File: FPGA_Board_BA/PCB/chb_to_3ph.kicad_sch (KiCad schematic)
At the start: 1 part, among them J103 Plug_Termincal_8pin

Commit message: lots of work
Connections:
- net Ph_A1_out renamed M_PHA
- net Ph_B1_out renamed M_PHB
- net Ph_C1_out renamed M_PHC
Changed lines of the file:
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@@
 		)
 	)
-	(wire
-		(pts
-			(xy 134.62 92.71) (xy 138.43 92.71)
-		)
-		(stroke
-			(width 0)
-			(type default)
-		)
-	)
-	(wire
-		(pts
-			(xy 118.11 92.71) (xy 121.92 92.71)
-		)
-		(stroke
-			(width 0)
-			(type default)
-		)
-	)
-	(wire
-		(pts
-			(xy 134.62 87.63) (xy 138.43 87.63)
-		)
-		(stroke
-			(width 0)
-			(type default)
-		)
-	)
-	(wire
-		(pts
-			(xy 134.62 85.09) (xy 138.43 85.09)
-		)
-		(stroke
-			(width 0)
-			(type default)
-		)
-	)
-	(wire
-		(pts
-			(xy 118.11 87.63) (xy 121.92 87.63)
-		)
-		(stroke
-			(width 0)
-			(type default)
-		)
-	)
-	(wire
-		(pts
-			(xy 134.62 90.17) (xy 138.43 90.17)
-		)
-		(stroke
-			(width 0)
-			(type default)
-		)
-	)
-	(wire
-		(pts
-			(xy 118.11 90.17) (xy 121.92 90.17)
-		)
-		(stroke
-			(width 0)
-			(type default)
-		)
-	)
-	(wire
-		(pts
-			(xy 118.11 85.09) (xy 121.92 85.09)
-		)
-		(stroke
-			(width 0)
-			(type default)
+	(junction
+		(at 139.7 87.63)
+		(diameter 0)
+		(color 0 0 0 0)
+	)
+	(junction
+		(at 137.16 90.17)
+		(diameter 0)
+		(color 0 0 0 0)
+	)
+	(junction
+		(at 142.24 85.09)
+		(diameter 0)
+		(color 0 0 0 0)
+	)
+	(wire
+		(pts
+			(xy 144.78 113.03) (xy 139.7 113.03)
+		)
+		(stroke
+			(width 0)
+			(type default)
+		)
+	)
+	(wire
+		(pts
+			(xy 134.62 92.71) (xy 146.05 92.71)
+		)
+		(stroke
+			(width 0)
+			(type default)
+		)
+	)
+	(wire
+		(pts
+			(xy 144.78 118.11) (xy 137.16 118.11)
+		)
+		(stroke
+			(width 0)
+			(type default)
+		)
+	)
+	(wire
+		(pts
+			(xy 110.49 92.71) (xy 121.92 92.71)
+		)
+		(stroke
+			(width 0)
+			(type default)
+		)
+	)
+	(wire
+		(pts
+			(xy 134.62 87.63) (xy 139.7 87.63)
+		)
+		(stroke
+			(width 0)
+			(type default)
+		)
+	)
+	(wire
+		(pts
+			(xy 139.7 87.63) (xy 146.05 87.63)
+		)
+		(stroke
+			(width 0)
+			(type default)
+		)
+	)
+	(wire
+		(pts
+			(xy 137.16 118.11) (xy 137.16 90.17)
+		)
+		(stroke
+			(width 0)
+			(type default)
+		)
+	)
+	(wire
+		(pts
+			(xy 134.62 85.09) (xy 142.24 85.09)
+		)
+		(stroke
+			(width 0)
+			(type default)
+		)
+	)
+	(wire
+		(pts
+			(xy 142.24 85.09) (xy 146.05 85.09)
+		)
+		(stroke
+			(width 0)
+			(type default)
+		)
+	)
+	(wire
+		(pts
+			(xy 110.49 87.63) (xy 121.92 87.63)
+		)
+		(stroke
+			(width 0)
+			(type default)
+		)
+	)
+	(wire
+		(pts
+			(xy 134.62 90.17) (xy 137.16 90.17)
+		)
+		(stroke
+			(width 0)
+			(type default)
+		)
+	)
+	(wire
+		(pts
+			(xy 144.78 107.95) (xy 142.24 107.95)
+		)
+		(stroke
+			(width 0)
+			(type default)
+		)
+	)
+	(wire
+		(pts
+			(xy 110.49 90.17) (xy 121.92 90.17)
+		)
+		(stroke
+			(width 0)
+			(type default)
+		)
+	)
+	(wire
+		(pts
+			(xy 142.24 107.95) (xy 142.24 85.09)
+		)
+		(stroke
+			(width 0)
+			(type default)
+		)
+	)
+	(wire
+		(pts
+			(xy 110.49 85.09) (xy 121.92 85.09)
+		)
+		(stroke
+			(width 0)
+			(type default)
+		)
+	)
+	(wire
+		(pts
+			(xy 137.16 90.17) (xy 146.05 90.17)
+		)
+		(stroke
+			(width 0)
+			(type default)
+		)
+	)
+	(wire
+		(pts
+			(xy 139.7 113.03) (xy 139.7 87.63)
+		)
+		(stroke
+			(width 0)
+			(type default)
+		)
+	)
+	(global_label "M_PHB"
+		(shape bidirectional)
+		(at 144.78 113.03 0)
+		(fields_autoplaced yes)
+		(effects
+			(font
+				(size 1.27 1.27)
+			)
+			(justify left)
+		)
+		(property "Intersheetrefs" "${INTERSHEET_REFS}"
+			(at 155.166 113.03 0)
+			(effects
+				(font
+					(size 1.27 1.27)
+				)
+				(justify left)
+				(hide yes)
+			)
+		)
+	)
+	(global_label "M_PHA"
+		(shape bidirectional)
+		(at 144.78 107.95 0)
+		(fields_autoplaced yes)
+		(effects
+			(font
+				(size 1.27 1.27)
+			)
+			(justify left)
+		)
+		(property "Intersheetrefs" "${INTERSHEET_REFS}"
+			(at 154.9846 107.95 0)
+			(effects
+				(font
+					(size 1.27 1.27)
+				)
+				(justify left)
+				(hide yes)
+			)
+		)
+	)
+	(global_label "M_PHC"
+		(shape bidirectional)
+		(at 144.78 118.11 0)
+		(fields_autoplaced yes)
+		(effects
+			(font
+				(size 1.27 1.27)
+			)
+			(justify left)
+		)
+		(property "Intersheetrefs" "${INTERSHEET_REFS}"
+			(at 155.166 118.11 0)
+			(effects
+				(font
+					(size 1.27 1.27)
+				)
+				(justify left)
+				(hide yes)
+			)
 		)
 	)
 	(hierarchical_label "Ph_A1_out"
 		(shape input)
-		(at 138.43 85.09 0)
+		(at 146.05 85.09 0)
 		(effects
 			(font
@@
 	(hierarchical_label "Ph_C1_out"
 		(shape input)
-		(at 138.43 90.17 0)
+		(at 146.05 90.17 0)
 		(effects
 			(font
@@
 	(hierarchical_label "Ph_D1_out"
 		(shape input)
-		(at 138.43 92.71 0)
+		(at 146.05 92.71 0)
 		(effects
 			(font
@@
 	(hierarchical_label "Ph_A2_out"
 		(shape input)
-		(at 118.11 85.09 180)
+		(at 110.49 85.09 180)
 		(effects
 			(font
@@
 	(hierarchical_label "Ph_D2_out"
 		(shape input)
-		(at 118.11 92.71 180)
+		(at 110.49 92.71 180)
 		(effects
 			(font
@@
 	(hierarchical_label "Ph_B2_out"
 		(shape input)
-		(at 118.11 87.63 180)
+		(at 110.49 87.63 180)
 		(effects
 			(font
@@
 	(hierarchical_label "Ph_C2_out"
 		(shape input)
-		(at 118.11 90.17 180)
+		(at 110.49 90.17 180)
 		(effects
 			(font
@@
 	(hierarchical_label "Ph_B1_out"
 		(shape input)
-		(at 138.43 87.63 0)
-		(effects
-			(font
+		(at 146.05 87.63 0)
+		(effects
+			(font

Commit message: work
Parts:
- renumbered J103 to J9
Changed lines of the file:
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@@
 		(dnp no)
 		(fields_autoplaced yes)
-		(property "Reference" "J103"
+		(property "Reference" "J9"
 			(at 128.27 78.74 0)
 			(effects
@@
 			(project "FPGA_Board_BA"
 				(path "/fd7503bc-e7fc-4766-b224-3d1c3d7de5ff/9a7bfc82-408b-4644-8882-19405b07f717"
-					(reference "J103")
+					(reference "J9")
 					(unit 1)
 				)

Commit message: Besprechung mit Leo
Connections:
- net M_PHA renamed Ph_A1_out
- net M_PHB renamed Ph_B1_out
- net M_PHC renamed Ph_C1_out
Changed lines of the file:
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@@
-		)
-	)
-	(junction
-		(at 139.7 87.63)
-		(diameter 0)
-		(color 0 0 0 0)
-	)
-	(junction
-		(at 137.16 90.17)
-		(diameter 0)
-		(color 0 0 0 0)
-	)
-	(junction
-		(at 142.24 85.09)
-		(diameter 0)
-		(color 0 0 0 0)
-	)
-	(wire
-		(pts
-			(xy 144.78 113.03) (xy 139.7 113.03)
-		)
-		(stroke
-			(width 0)
-			(type default)
 		)
 	)
@@
 		(pts
 			(xy 134.62 92.71) (xy 146.05 92.71)
-		)
-		(stroke
-			(width 0)
-			(type default)
-		)
-	)
-	(wire
-		(pts
-			(xy 144.78 118.11) (xy 137.16 118.11)
 		)
 		(stroke
@@
 	(wire
 		(pts
-			(xy 134.62 87.63) (xy 139.7 87.63)
+			(xy 134.62 87.63) (xy 146.05 87.63)
 		)
 		(stroke
@@
 	(wire
 		(pts
-			(xy 139.7 87.63) (xy 146.05 87.63)
-		)
-		(stroke
-			(width 0)
-			(type default)
-		)
-	)
-	(wire
-		(pts
-			(xy 137.16 118.11) (xy 137.16 90.17)
-		)
-		(stroke
-			(width 0)
-			(type default)
-		)
-	)
-	(wire
-		(pts
-			(xy 134.62 85.09) (xy 142.24 85.09)
-		)
-		(stroke
-			(width 0)
-			(type default)
-		)
-	)
-	(wire
-		(pts
-			(xy 142.24 85.09) (xy 146.05 85.09)
+			(xy 134.62 85.09) (xy 146.05 85.09)
 		)
 		(stroke
@@
 	(wire
 		(pts
-			(xy 134.62 90.17) (xy 137.16 90.17)
-		)
-		(stroke
-			(width 0)
-			(type default)
-		)
-	)
-	(wire
-		(pts
-			(xy 144.78 107.95) (xy 142.24 107.95)
+			(xy 134.62 90.17) (xy 146.05 90.17)
 		)
 		(stroke
@@
 	(wire
 		(pts
-			(xy 142.24 107.95) (xy 142.24 85.09)
-		)
-		(stroke
-			(width 0)
-			(type default)
-		)
-	)
-	(wire
-		(pts
 			(xy 110.49 85.09) (xy 121.92 85.09)
 		)
@@
 		)
 	)
-	(wire
-		(pts
-			(xy 137.16 90.17) (xy 146.05 90.17)
-		)
-		(stroke
-			(width 0)
-			(type default)
-		)
-	)
-	(wire
-		(pts
-			(xy 139.7 113.03) (xy 139.7 87.63)
-		)
-		(stroke
-			(width 0)
-			(type default)
-		)
-	)
-	(global_label "M_PHB"
-		(shape bidirectional)
-		(at 144.78 113.03 0)
-		(fields_autoplaced yes)
-		(effects
-			(font
-				(size 1.27 1.27)
-			)
-			(justify left)
-		)
-		(property "Intersheetrefs" "${INTERSHEET_REFS}"
-			(at 155.166 113.03 0)
-			(effects
-				(font
-					(size 1.27 1.27)
-				)
-				(justify left)
-				(hide yes)
-			)
-		)
-	)
-	(global_label "M_PHA"
-		(shape bidirectional)
-		(at 144.78 107.95 0)
-		(fields_autoplaced yes)
-		(effects
-			(font
-				(size 1.27 1.27)
-			)
-			(justify left)
-		)
-		(property "Intersheetrefs" "${INTERSHEET_REFS}"
-			(at 154.9846 107.95 0)
-			(effects
-				(font
-					(size 1.27 1.27)
-				)
-				(justify left)
-				(hide yes)
-			)
-		)
-	)
-	(global_label "M_PHC"
-		(shape bidirectional)
-		(at 144.78 118.11 0)
-		(fields_autoplaced yes)
-		(effects
-			(font
-				(size 1.27 1.27)
-			)
-			(justify left)
-		)
-		(property "Intersheetrefs" "${INTERSHEET_REFS}"
-			(at 155.166 118.11 0)
-			(effects
-				(font
-					(size 1.27 1.27)
-				)
-				(justify left)
-				(hide yes)
-			)
-		)
-	)

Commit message: exported stuff
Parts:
- removed J9: Plug_Termincal_8pin, MYLIB_Misc:DMC 1,5_ 8-G1-3,5 P20THR, symbol MYLIB_Misc:Plug_Termincal_8pin
- added J21: Plug_Terminal_2x4pin, MYLIB_Misc:DMC 1,5_ 8-G1-3,5 P20THR, symbol MYLIB_Misc:Plug_Terminal_2x4pin
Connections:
- net Ph_A1_out: now also J21.2 (Pin_2)
- net Ph_A2_out: now also J21.1 (Pin_1)
- net Ph_B1_out: now also J21.4 (Pin_4)
- net Ph_B2_out: now also J21.3 (Pin_3)
- net Ph_C1_out: now also J21.6 (Pin_6)
- net Ph_C2_out: now also J21.5 (Pin_5)
- net Ph_D1_out: now also J21.8 (Pin_8)
- net Ph_D2_out: now also J21.7 (Pin_7)
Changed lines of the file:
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@@
 	)
 	(symbol
-		(lib_id "MYLIB_Misc:Plug_Termincal_8pin")
+		(lib_id "MYLIB_Misc:Plug_Terminal_2x4pin")
 		(at 128.27 85.09 0)
 		(unit 1)
@@
 		(dnp no)
 		(fields_autoplaced yes)
-		(property "Reference" "J9"
+		(property "Reference" "J21"
 			(at 128.27 78.74 0)
 			(effects
@@
 			)
 		)
-		(property "Value" "Plug_Termincal_8pin"
+		(property "Value" "Plug_Terminal_2x4pin"
 			(at 128.27 81.28 0)
 			(effects
@@
 			)
 		)
-		(pin "7"
+		(pin "5"
 		)
 		(pin "8"
 		)
-		(pin "4"
+		(pin "6"
 		)
-		(pin "6"
+		(pin "2"
 		)
 		(pin "3"
@@
 		(pin "1"
 		)
-		(pin "2"
+		(pin "7"
 		)
-		(pin "5"
+		(pin "4"
 		)
 		(instances
-			(project "FPGA_Board_BA"
+			(project ""
 				(path "/fd7503bc-e7fc-4766-b224-3d1c3d7de5ff/9a7bfc82-408b-4644-8882-19405b07f717"
-					(reference "J9")
+					(reference "J21")
 					(unit 1)
 				)

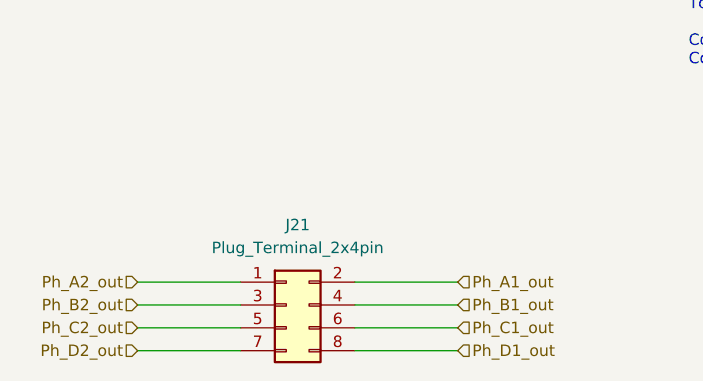
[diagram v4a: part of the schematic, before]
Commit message: component placement with new concept is ready
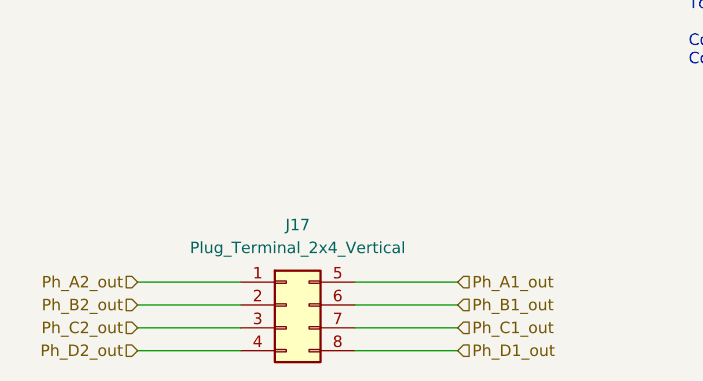
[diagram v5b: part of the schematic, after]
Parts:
- removed J21: Plug_Terminal_2x4pin, MYLIB_Misc:DMC 1,5_ 8-G1-3,5 P20THR, symbol MYLIB_Misc:Plug_Terminal_2x4pin
- added J17: Plug_Terminal_2x4_Vertical, MYLIB_Misc:Plug_Terminal_2x4_Vertical, symbol MYLIB_Misc:Plug_Terminal_2x4_Vertical
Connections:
- net Ph_A1_out: now also J17.5 (Pin_2)
- net Ph_A2_out: now also J17.1 (Pin_1)
- net Ph_B1_out: now also J17.6 (Pin_4)
- net Ph_B2_out: now also J17.2 (Pin_3)
- net Ph_C1_out: now also J17.7 (Pin_6)
- net Ph_C2_out: now also J17.3 (Pin_5)
- net Ph_D1_out: now also J17.8 (Pin_8)
- net Ph_D2_out: now also J17.4 (Pin_7)
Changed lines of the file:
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@@
 	)
 	(symbol
-		(lib_id "MYLIB_Misc:Plug_Terminal_2x4pin")
-		(at 128.27 85.09 0)
+		(lib_id "MYLIB_Misc:Plug_Terminal_2x4_Vertical")
+		(at 128.27 88.9 0)
 		(unit 1)
 		(exclude_from_sim no)
@@
 		(dnp no)
 		(fields_autoplaced yes)
-		(property "Reference" "J21"
+		(property "Reference" "J17"
 			(at 128.27 78.74 0)
 			(effects
@@
 			)
 		)
-		(property "Value" "Plug_Terminal_2x4pin"
+		(property "Value" "Plug_Terminal_2x4_Vertical"
 			(at 128.27 81.28 0)
 			(effects
@@
 			)
 		)
-		(property "Footprint" "MYLIB_Misc:DMC 1,5_ 8-G1-3,5 P20THR"
-			(at 127.508 65.786 0)
+		(property "Footprint" "MYLIB_Misc:Plug_Terminal_2x4_Vertical"
+			(at 128.27 65.024 0)
 			(effects
 				(font
@@
 			)
 		)
-		(property "Datasheet" "https://product-download.phoenixcontact.com/7581871?response-content-disposition=inline;%20filename%3D%221786895_02_en_00.pdf%22&Expires=1762790272&Signature=swgT~pfHFsm~KFte~1FyTUdCZaY3mURW7Sm3ZO1670aosCFDktyp77XVjT~WM-BF5UAYAn7SB97Gn5JYnUQEo2Fo4coNlwQu8FvGxlAgu6cPDUpTS7qKwCUFJAfHbnWDITx10Xgr4f3IGJZgshPlJKuMwfqJ1~soOFux2NQtmqne1nW1QpnapOHvfXEmIqUT8lfI05sqOMTbP8aHqqhzBDIfpY8psZXo36OHFrhnt8hDQ0wXe394Nf9wPZgUL--r-V-FA68hmgIiKUjjxetMxbp5wlmyiyZTnTkfqKPBXq4SCTPMeVpkhphIF7vmWwvwFFSD8XTuiqvSgzKTNBIHtQ__&Key-Pair-Id=K1I2N54A7B0GD"
-			(at 128.778 74.93 0)
+		(property "Datasheet" "https://www.mouser.de/datasheet/3/507/8/phoenix_contact_1787221_en.pdf"
+			(at 128.016 71.12 0)
 			(effects
 				(font
@@
 			)
 		)
-		(property "Description" "Pluggable Terminal Blocks 8 Pos 3.5mm Dbl Row Plug 24-16AWG Spring"
-			(at 127.762 78.232 0)
+		(property "Description" "Vertical 2x4 pin, 8A max 160V max"
+			(at 128.778 73.914 0)
 			(effects
 				(font
@@
 			)
 		)
-		(property "Mating Connector Mouser" " 651-1790357"
-			(at 129.286 68.58 0)
+		(property "Socket Mouser" "651-1787221"
+			(at 128.016 69.088 0)
 			(effects
 				(font
@@
 			)
 		)
-		(property "Mating Connector Link" "https://product-download.phoenixcontact.com/8945604?response-content-disposition=inline;%20filename%3D%221790357_04_en_03.pdf%22&Expires=1762789986&Signature=ipEMNH2oRldeatNpCt2LgQ2qfu7zONe9r5fTnUSu~jVXEFxJXimB1mNBJG54W6gMaB3mL1auhUEZHbNWKHeBpVePo4wLkQTSMGiAroKySyTr75NkMuRgQrBNp5zFPa0nsk04bgnmTglvgn3Nkk0r-ygqga5CCZms3pwphqmh2MiSRDj1dVFlWYrLZMXfeWBeOA8eRxkTpTCFV9F7L5cZnVIsq0jCQRITzgdzqH05q~PF1m-rPiv5SdIFT0eLthdpIX2QoY37c2J4~ZpfG3fvrBenTcVOu77f1kcfo4KCglyWA8fQXeP5CE9fn8rCtQ8mClfe-vR81PjWTNgBQX~ynw__&Key-Pair-Id=K1I2N54A7B0GD"
-			(at 128.778 71.628 0)
+		(property "Header Mouser" "651-1790124"
+			(at 127.762 67.056 0)
 			(effects
 				(font
@@
 			)
 		)
-		(pin "5"
+		(pin "1"
+		)
+		(pin "7"
+		)
+		(pin "2"
+		)
+		(pin "3"
 		)
 		(pin "8"
@@
 		(pin "6"
 		)
-		(pin "2"
+		(pin "4"
 		)
-		(pin "3"
-		)
-		(pin "1"
-		)
-		(pin "7"
-		)
-		(pin "4"
+		(pin "5"
 		)
 		(instances
 			(project ""
 				(path "/fd7503bc-e7fc-4766-b224-3d1c3d7de5ff/9a7bfc82-408b-4644-8882-19405b07f717"
-					(reference "J21")
+					(reference "J17")
 					(unit 1)
 				)
